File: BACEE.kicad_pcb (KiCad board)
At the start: 2 copper layers, 41.1 x 24.8 mm, 17 parts, among them J1 Serial Port, J2 Digital pins, J3 I2C, J4 ISCP, U1 24LC1025, U2 DS1337S+, U3 24LC1025, U4 ATMEGA328-AU, Y1 Crystal 32KHz, Y2 Crystal 16MHz

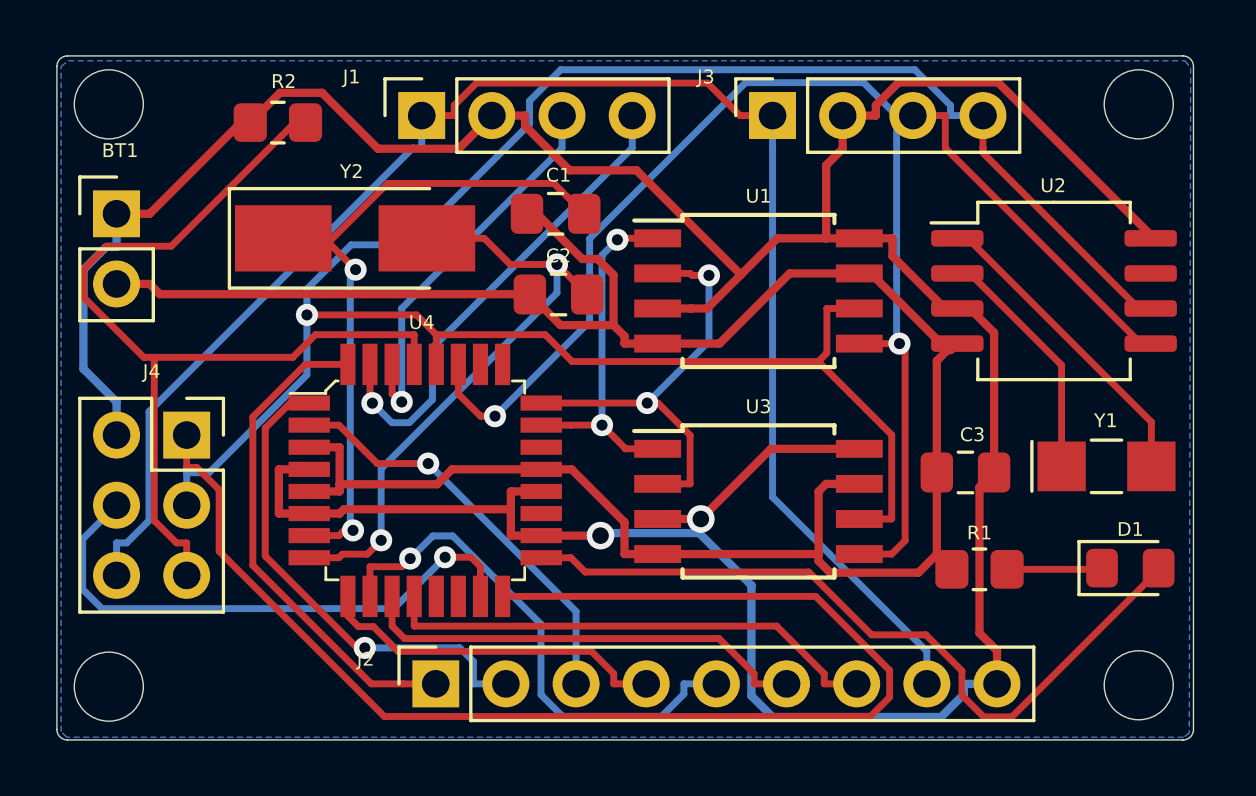
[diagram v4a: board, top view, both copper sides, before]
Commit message: Completed front and back silk screens.
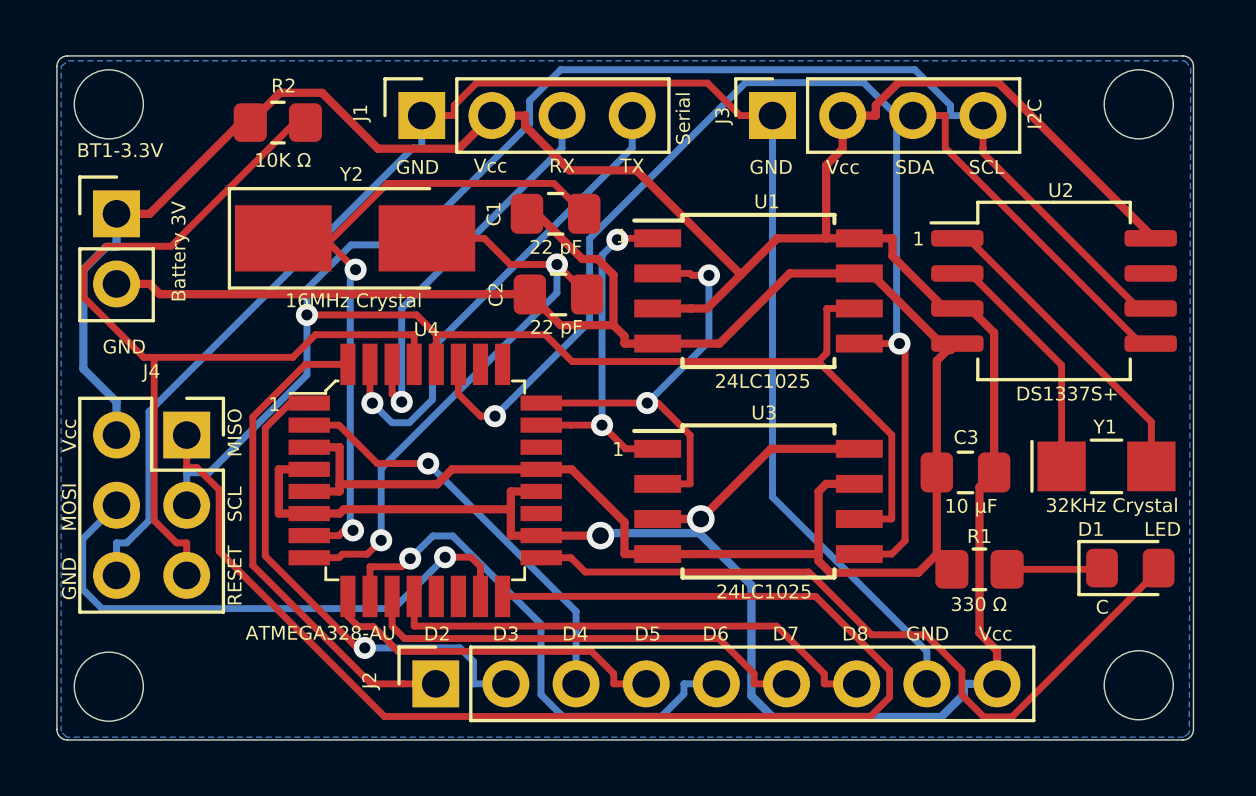
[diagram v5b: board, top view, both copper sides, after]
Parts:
- added G***: LOGO, dtl:Lutzcraft_logo_500DPI, B.Cu at (101.7, 102.7)
- added REF**: OSHW-Logo2_14.6x12mm_SilkScreen, Symbol:OSHW-Logo2_14.6x12mm_SilkScreen, B.Cu at (88.6, 103.9)
- added REF**: KiCad-Logo2_6mm_SilkScreen, Symbol:KiCad-Logo2_6mm_SilkScreen, B.Cu at (78.4, 107.1)
- Y2: value Crystal 16MHz -> 16MHz Crystal
- renumbered BT1 to BT1-3.3V
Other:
- board text added: "1"
- board text added: "10 μF"
- board text added: "22 pF"
- board text added: "24LC1025"
- board text added: "32KHz Crystal"
- board text added: "330 Ω"
- board text added: "Arduino clone with: - 2Mbit EEPROM - Clock and calendar - I2C, SPI, GPIO"
- board text added: "C"
- board text added: "D2"
- board text added: "D3"
- board text added: "D4"
- board text added: "D5"
- board text added: "D6"
- board text added: "D7"
- board text added: "D8"
- board text added: "DS1337S+"
- board text added: "GND"
- board text added: "I2C"
- board text added: "LED"
- board text added: "MISO"
- board text added: "MOSI"
- board text added: "RESET"
- board text added: "RX"
- board text added: "SCL"
- board text added: "SDA"
- board text added: "Serial"
- board text added: "TX"
- board text added: "Vcc"
- board text added: "dlutz52@gmail.com"
